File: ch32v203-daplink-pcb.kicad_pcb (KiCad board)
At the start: 2 copper layers, 47 x 17.8 mm, 29 parts, among them J1 USB2.0_C_v3, J2 DAPLink-SWD-Send-10Pin, J3 DAPLink-SWD-Send-6Pin, M2-1 M2-Hole, M2-2 M2-Hole, M2-3 M2-Hole, M2-4 M2-Hole, U1 STM32V103C8T6, U2 AMS1117-3.3, Y2 8M

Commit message: v1.0.0
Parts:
- added REF**: JLCJLCJLCJLC, $74th:JLCJLCJLCJLC, B.Cu at (67.8, 24.1)
- R6, R7: moved to B.Cu
- moved C5 1.27 mm to (74.3, 27.9)
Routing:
- net GND: track 45.2 -> 42.9 mm, vias 45 -> 47
- net +5V: track 76.5 -> 77.6 mm
- net Net-(J1-CC1): track 3.17 -> 3.12 mm, vias 0 -> 1
- net Net-(J1-CC2): vias 0 -> 1
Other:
- board text added: "74TH-DL-v1.0.0"
- board text added: "CH32V203"
- board text added: "DAP Link"

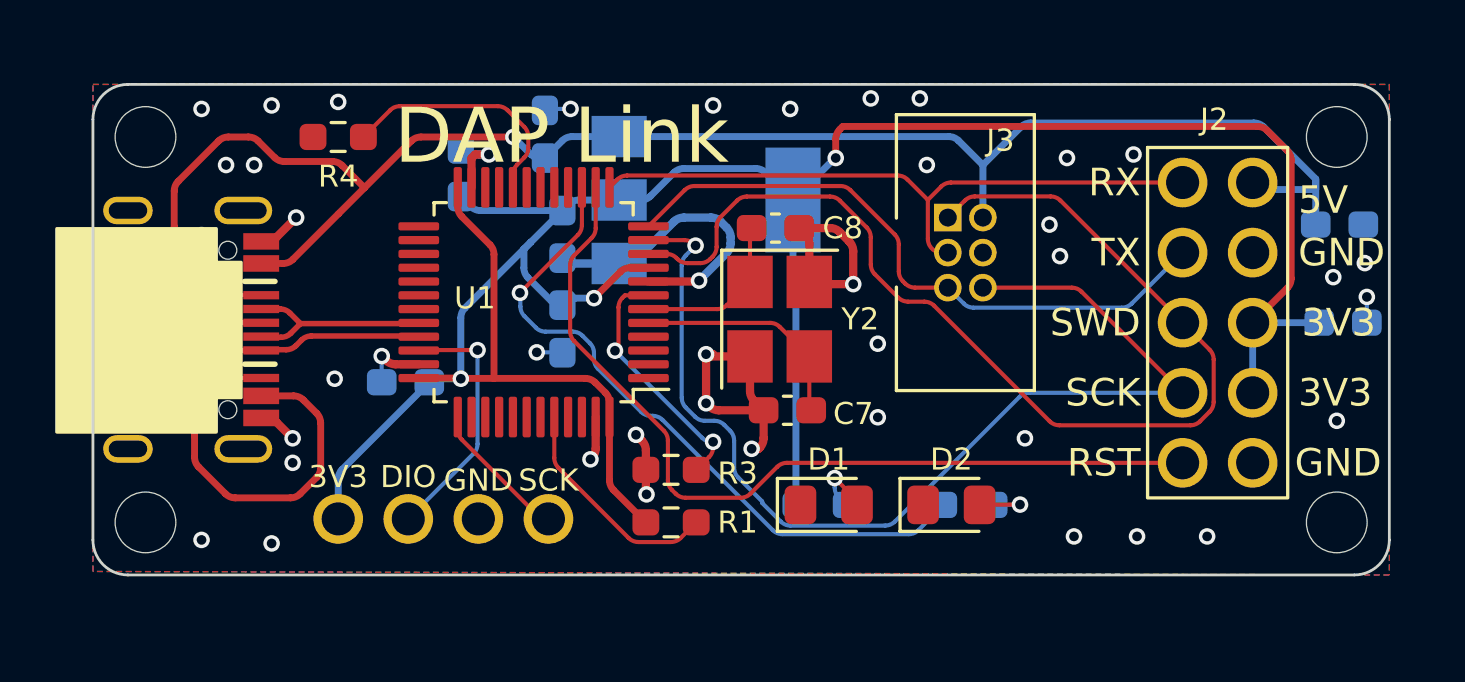
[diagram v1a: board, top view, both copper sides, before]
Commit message: for Arduino UNO R4
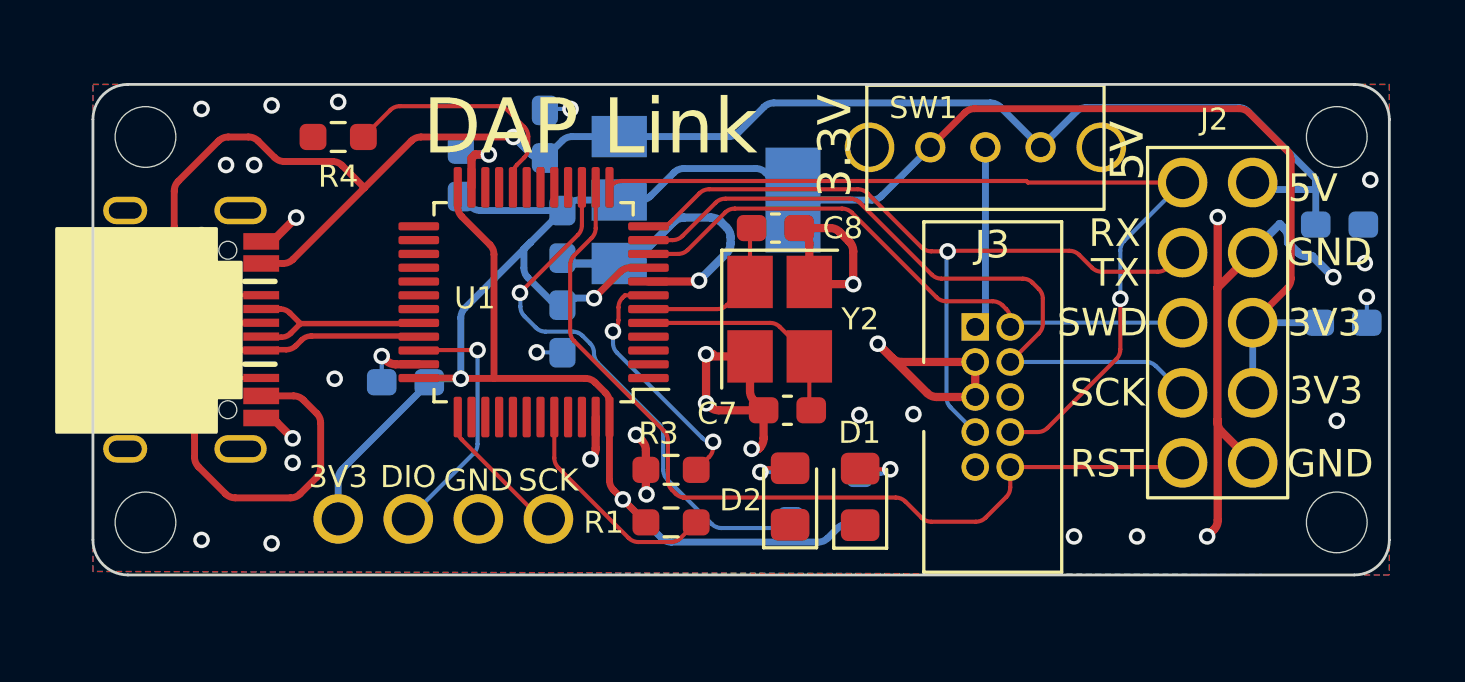
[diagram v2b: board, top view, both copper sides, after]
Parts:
- added SW1: SW_SPDT, $74th:Slide_Switch, F.Cu at (61.6, 25.1)
- J3: footprint $74th:BoxPinHeader_2x03_P1.27mm_Vertical -> $74th:BoxPinHeader_2x05_P1.27mm_Vertical
- moved R2 6.47 mm to (54.5, 37.8), turned to 90 degrees
- moved D2 5.85 mm to (54.5, 37.8), turned to 90 degrees
- moved J3 5.33 mm to (61.8, 34.2)
- moved R8 1.41 mm to (57.0, 37.9), turned to 90 degrees
- moved D1 1.18 mm to (57.0, 37.8), turned to 90 degrees
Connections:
- J3 pad 1: SWD_DIO -> VCC
- J3 pad 2: +5V -> SWD_DIO
- J3 pad 3: CDC_RXD -> GND
- J3 pad 4: GND -> SWD_CLK
- J3 pad 5: CDC_TXD -> GND
- J3 pad 6: SWD_CLK -> unconnected-(J3-NC-Pad6)
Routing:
- net GND: track 42.9 -> 72.2 mm, vias 47 -> 40
- net SWD_DIO: track 40.7 -> 22.0 mm
- net SWD_CLK: track 39.1 -> 25.8 mm, vias 1 -> 0
- net CDC_RXD: track 23.9 -> 33.1 mm, vias 0 -> 1
- net VCC: track 0.00 -> 6.64 mm
- net LED_SWD: track 24.7 -> 19.6 mm
- net CDC_TXD: track 23.3 -> 28.3 mm, vias 0 -> 1
- net +3V3: track 97.4 -> 95.8 mm
- net SWD_RST: track 31.8 -> 33.1 mm
- net +5V: track 77.6 -> 76.6 mm
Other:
- board text added: "3.3V"
- board text added: "5V"
- board text added: "74TH-DL-v1.1.0"
- board text removed: "74TH-DL-v1.0.0"

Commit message: v1.1.0
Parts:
- J3: renamed from J2; footprint $74th:DAPLink-SWD -> $74th:Side-2x5P-PinHeader-Right
- moved C4 9.78 mm to (64.5, 27.9), turned to 180 degrees
- moved C3 9.71 mm to (64.7, 31.2), turned to 90 degrees
- moved J3 2.17 mm to (72.1, 31.8)
- moved M3 1.91 mm to (72.4, 24.6)
- moved M4 1.91 mm to (72.4, 38.7)
- renumbered C8 to C1, C7 to C2, C6 to C3, C5 to C4, C10 to C5, C3 to C6, C9 to C7, C2 to C8, C4 to C9, D2 to D1, D1 to D2, J3 to J2, M2-3 to M1, M2-2 to M2, M2-1 to M3, M2-4 to M4, R4 to R1, R3 to R2, R1 to R3, R8 to R4, R2 to R5, R7 to R6, R6 to R7, Y2 to Y1
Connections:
- J3 pad 10: +5V -> GND
- J3 pad 2: CDC_TXD -> +5V
- J3 pad 3: SWD_DIO -> CDC_TXD
- J3 pad 4: SWD_CLK -> GND
- J3 pad 5: SWD_RST -> SWD_DIO
- J3 pad 6: GND -> +3V3
- J3 pad 7: +3V3 -> SWD_CLK
- J3 pad 9: GND -> SWD_RST
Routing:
- net GND: track 72.2 -> 57.6 mm, vias 40 -> 47
- net CDC_TXD: track 28.3 -> 35.3 mm
- net SWD_DIO: track 22.0 -> 26.6 mm, vias 0 -> 1
- net +3V3: track 95.8 -> 99.6 mm, vias 3 -> 4
- net CDC_RXD: track 33.1 -> 36.7 mm, vias 1 -> 3
- net SWD_CLK: track 25.8 -> 29.3 mm, vias 0 -> 1
- net SWD_RST: track 33.1 -> 36.6 mm
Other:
- board size 47 x 17.8 mm -> 45.2 x 17.8 mm
- board text added: "3V3"
- board text added: "GND"
- board text added: "RST"
- board text added: "RXD"
- board text added: "SCK"
- board text added: "SWD"
- board text added: "TXD"
